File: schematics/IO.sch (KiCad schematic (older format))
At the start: 78 parts, among them J4 Outputs, J8 Power Pins, Q1 MMBT3906, U10 TL082, U11 6S21, U12 6S21, U13 TL082, U16 TL082, U6 DS1307Z+, U7 LM324, U8 TL082, U9 MCP4728, Y1 32.768 kHz

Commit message: fix: increased cutoff frequency
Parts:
- C23, C29: value 3p3 -> 0.5p
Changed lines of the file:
@@
 AR Path="/54260FB5/5441D502" Ref="C29"  Part="1"
 F 0 "C29" H 10075 2475 40  0000 L CNN
-F 1 "3p3" H 10081 2290 40  0000 L CNN
+F 1 "0.5p" H 10081 2290 40  0000 L CNN
 F 2 "Capacitors_SMD:C_0603" H 10113 2225 30  0001 C CNN
 F 3 "" H 10075 2375 60  0000 C CNN
@@
 AR Path="/54260FB5/55B7C49A" Ref="C23"  Part="1"
 F 0 "C23" H 10150 1175 40  0000 L CNN
-F 1 "3p3" H 10156 990 40  0000 L CNN
+F 1 "0.5p" H 10156 990 40  0000 L CNN
 F 2 "Capacitors_SMD:C_0603" H 10188 925 30  0001 C CNN
 F 3 "" H 10150 1075 60  0000 C CNN

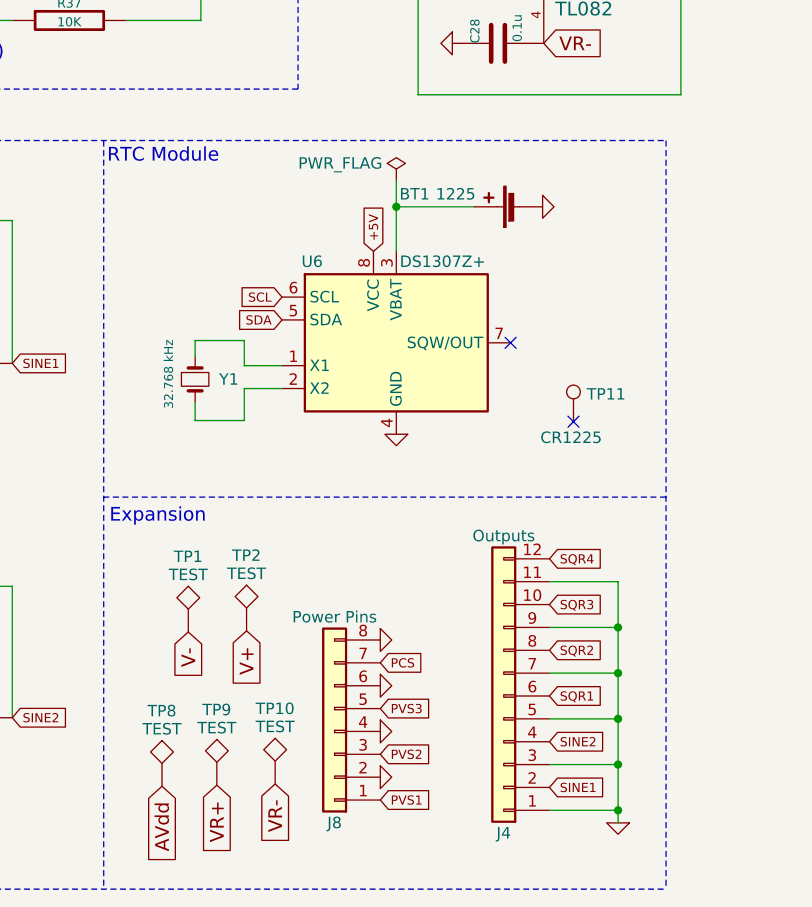
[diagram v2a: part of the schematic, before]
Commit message: feat: external power circuit schematics
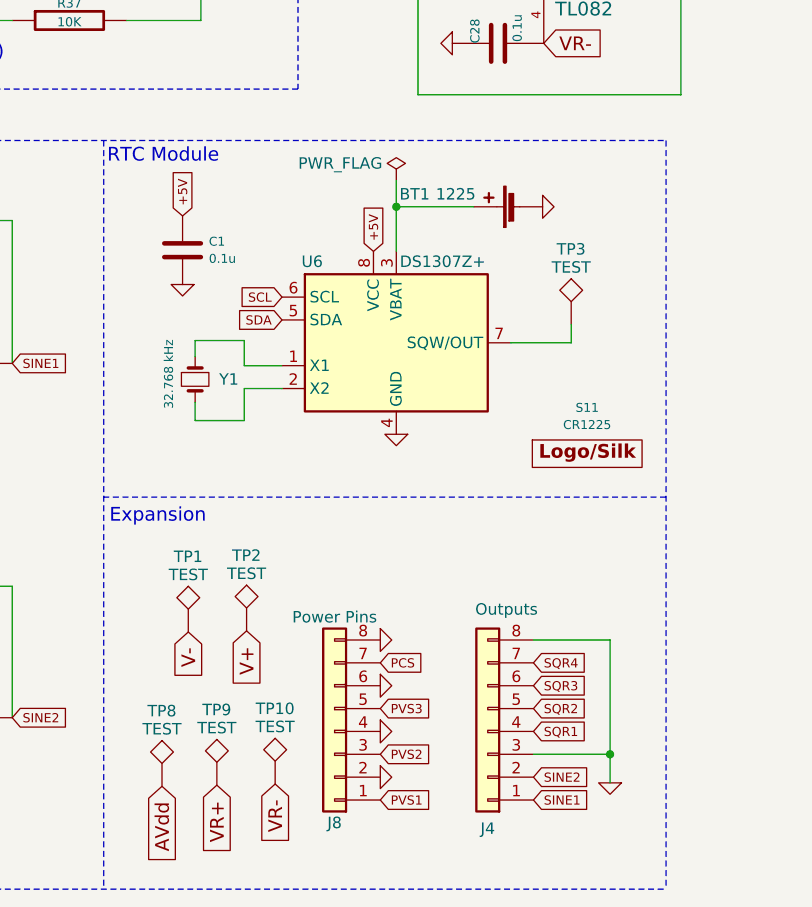
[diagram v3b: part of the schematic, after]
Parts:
- removed J4: Outputs, Pin_Headers:Pin_Header_Straight_1x12_Pitch2.54mm, symbol PSLab-rescue:Conn_01x12
- removed TP11: CR1225, Battery:Battery_CR1225, symbol Connector:TestPoint
- added C1: 0.1u, Capacitor_SMD:C_0603_1608Metric, symbol Device:C
- added J4: Outputs, Connector_PinSocket_2.54mm:PinSocket_1x08_P2.54mm_Vertical, symbol Connector_Generic:Conn_01x08
- added S11: CR1225, Battery:Battery_CR1225, symbol PSLab:Logos
- added TP3: TEST, TestPoint:TestPoint_Pad_1.0x1.0mm, symbol PSLab-rescue:TEST
- C22, C23, C24, C25, C26, C27, C28, C29, C30, C31, C32, C33, C34, C35, C36, C37, C38, C39, C40, C41, C43, C6, C7: footprint Capacitors_SMD:C_0603 -> Capacitor_SMD:C_0603_1608Metric
- R14, R15, R16, R17, R18, R19, R20, R21, R22, R23, R24, R25, R26, R27, R28, R29, R30, R31, R32, R33, R34, R35, R36, R37, R38, R39, R40, R41, R42, R43, R44, R45, R46, R47, R50: footprint Resistors_SMD:R_0603 -> Resistor_SMD:R_0603_1608Metric
- TP1, TP10, TP2, TP8, TP9: footprint Measurement_Points:Measurement_Point_Round-SMD-Pad_Small -> TestPoint:TestPoint_Pad_1.0x1.0mm
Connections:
- net +5V: now also C1.1
- net GND: now also C1.2, J4.3 (Pin_3), J4.8 (Pin_8)
- net SINE1: now also J4.1 (Pin_1)
- net SINE2: now also J4.2 (Pin_2)
- net SQR1: now also J4.4 (Pin_4)
- net SQR2: now also J4.5 (Pin_5)
- net SQR3: now also J4.6 (Pin_6)
- net SQR4: now also J4.7 (Pin_7)
- net at U6.7 (SQW/OUT): now also TP3.1
- no-connect marks 3 -> 1

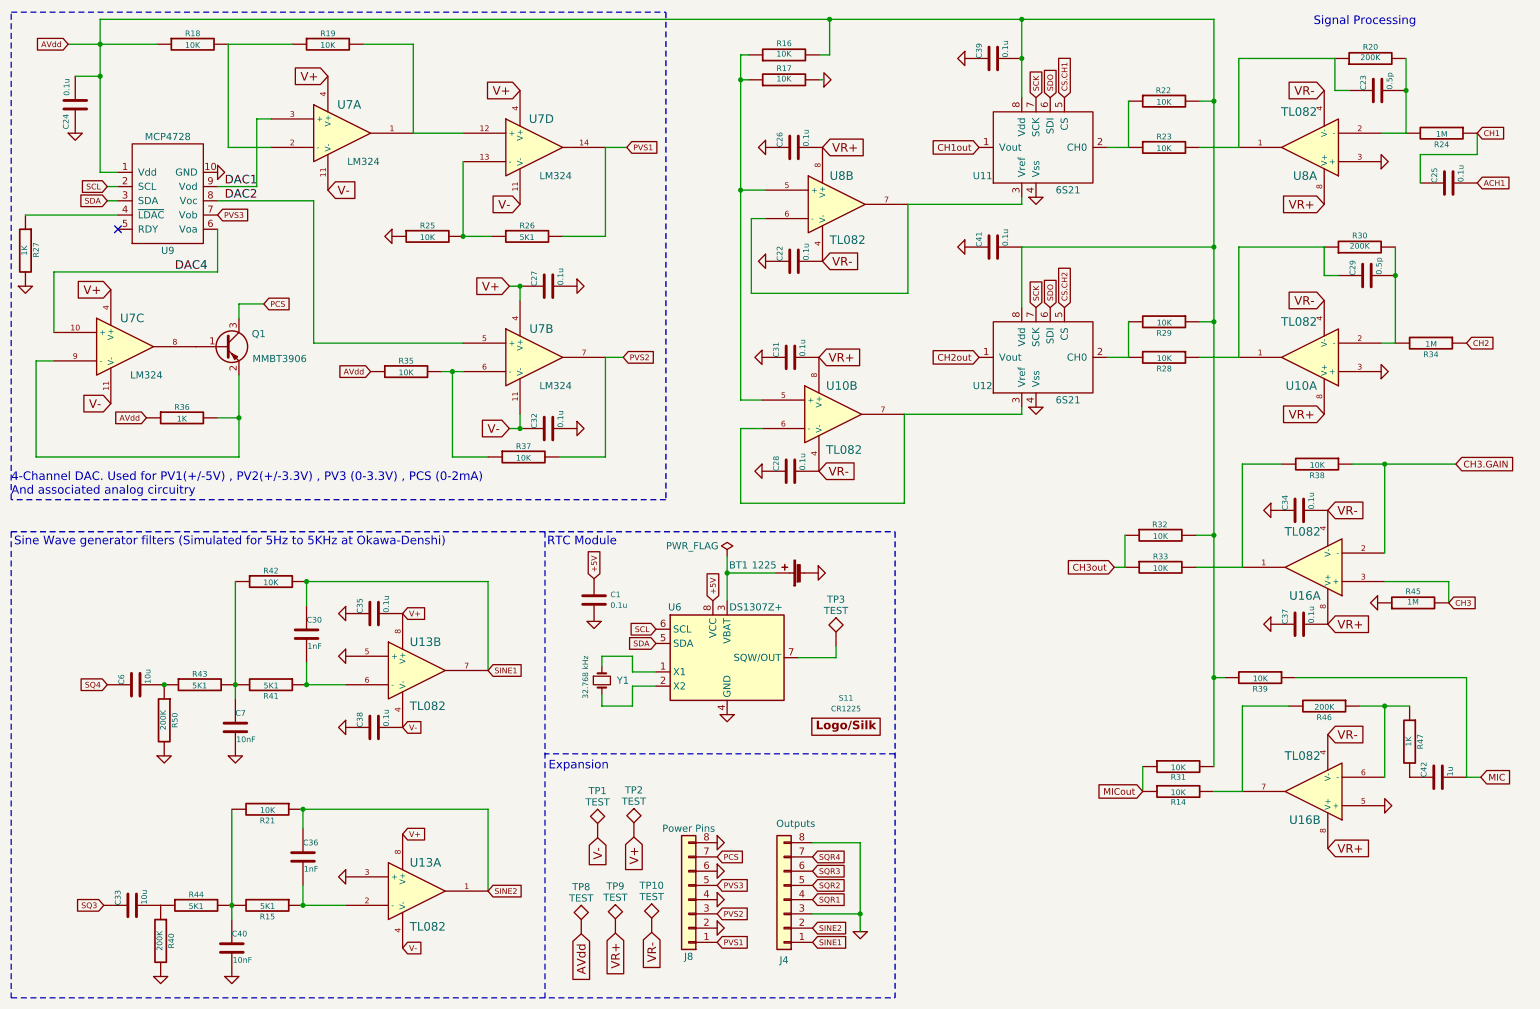
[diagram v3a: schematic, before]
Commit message: refactor: fixed rotation in resistors
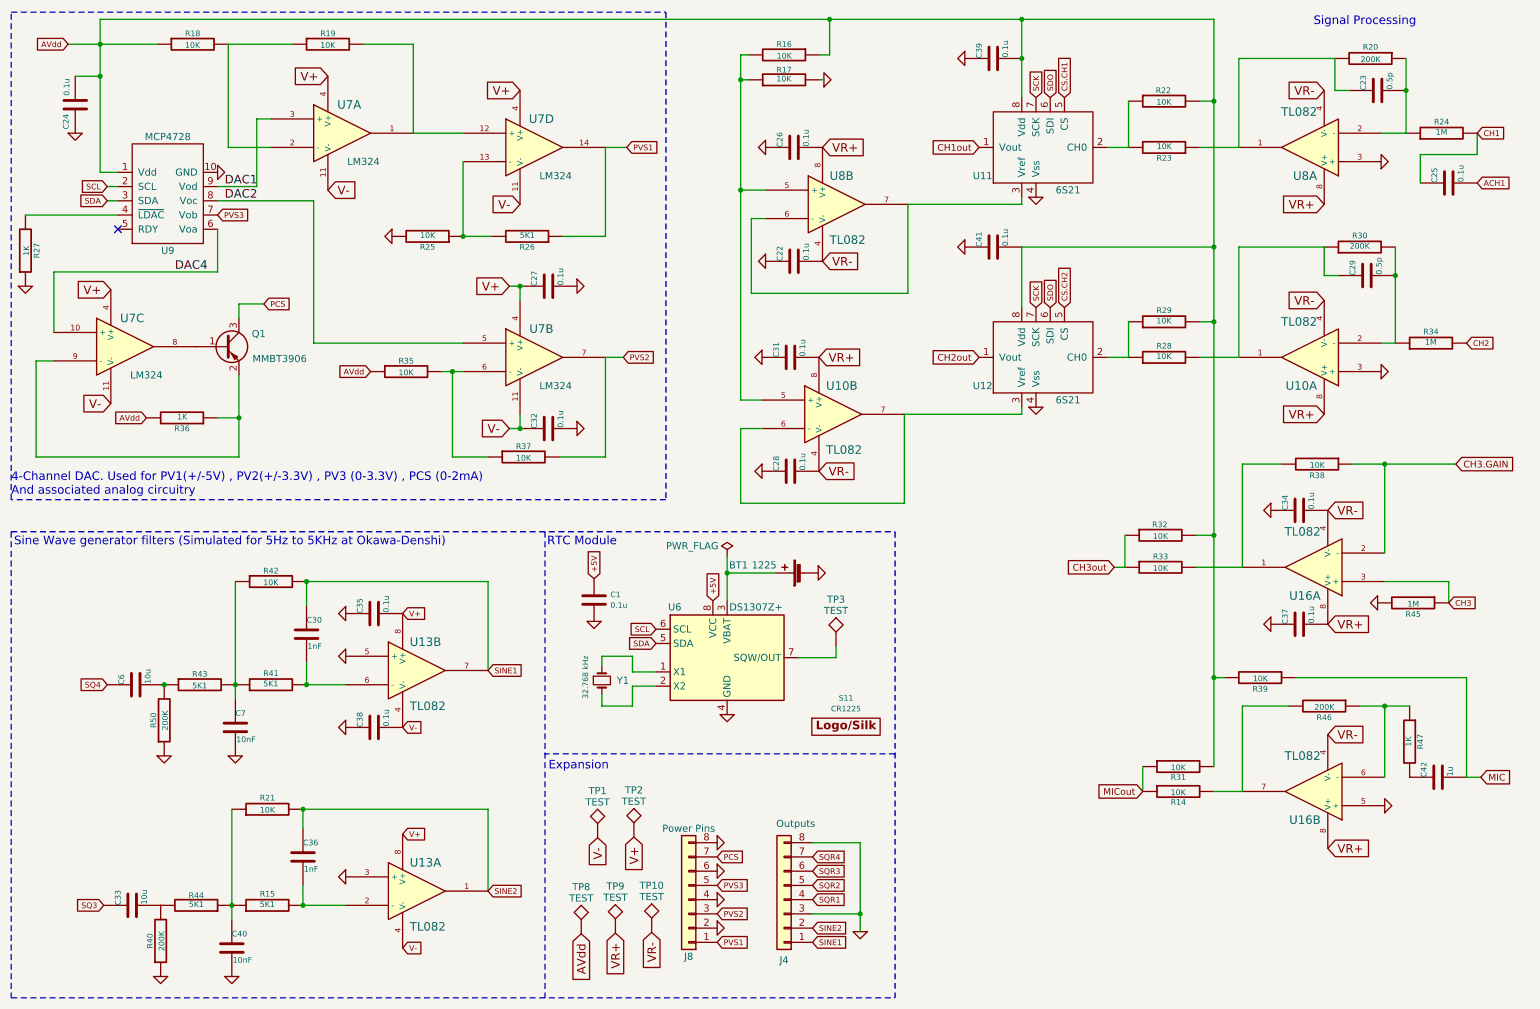
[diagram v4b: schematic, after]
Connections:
- net AVdd: now also R16.1, R29.2, R36.2; no longer R16.2, R29.1, R36.1
- net CH1: now also R24.2; no longer R24.1
- net CH2: now also R34.2; no longer R34.1
- net CH3: now also R45.1; no longer R45.2
- net GND: now also R25.2, R27.1, R40.1, R45.2, R50.1; no longer R25.1, R27.2, R40.2, R45.1, R50.2
- net PVS1: now also R26.1; no longer R26.2
- net SINE2: now also R21.2; no longer R21.1
- net at C29.1, R30.1, U10.1: now also R28.2; no longer R28.1
- net at C29.2, R30.2, U10.2 (-): now also R34.1; no longer R34.2
- net at R17.1, U10.5 (+), U8.5 (+): now also R16.2; no longer R16.1
- net at Q1.2 (E), U7.9 (-): now also R36.1; no longer R36.2
- net at U9.4 (~LDAC): now also R27.2; no longer R27.1
- net at C7.1, R42.1, R43.2: now also R41.1; no longer R41.2
- net at C6.2, R43.1: now also R50.2; no longer R50.1
- net at C23.1, U8.1: now also R20.2, R23.1; no longer R20.1, R23.2
- net at C23.2, U8.2 (-): now also R20.1, R24.1; no longer R20.2, R24.2
- net at R22.1, U11.2 (CH0): now also R23.2; no longer R23.1
- net at C30.2, U13.6 (-): now also R41.2; no longer R41.1
- net at C36.2, U13.2 (-): now also R15.2; no longer R15.1
- new net: R25.1, R26.2, U7.13 (-)
- new net: C33.2, R40.2, R44.2
- new net: C40.1, R15.1, R21.1, R44.1
- new net: R28.1, R29.1, U12.2 (CH0)
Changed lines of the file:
@@
 F 3 "" H 10525 2850 30  0000 C CNN
 	1    10525 2850
-	0    1    1    0
+	0    -1   -1   0
 $EndComp
 $Comp
@@
 AR Path="/555FFE64" Ref="R27"  Part="1"
 AR Path="/54260FB5/555FFE64" Ref="R27"  Part="1"
-F 0 "R27" V 575 2205 40  0000 C CNN
+F 0 "R27" V 730 2200 40  0000 C CNN
 F 1 "1K" V 657 2201 40  0000 C CNN
 F 2 "Resistor_SMD:R_0603_1608Metric" V 580 2200 30  0001 C CNN
 F 3 "" H 650 2200 30  0000 C CNN
 	1    650  2200
-	-1   0    0    -1
+	1    0    0    1
 $EndComp
 Text GLabel 950  750  0    40   Input ~ 0
@@
 F 3 "" H 4175 2100 30  0000 C CNN
 	1    4175 2100
-	0    -1   1    0
+	0    1    -1   0
 $EndComp
 $Comp
@@
 F 3 "" H 3475 2100 30  0000 C CNN
 	1    3475 2100
-	0    -1   1    0
+	0    1    -1   0
 $EndComp
 $Comp
@@
 F 3 "" H 1750 3375 30  0000 C CNN
 	1    1750 3375
-	0    -1   1    0
+	0    1    -1   0
 $EndComp
 Text GLabel 1500 3375 0    40   Input ~ 0
@@
 F 3 "" H 1600 7050 30  0000 C CNN
 	1    1600 7050
-	-1   0    0    -1
+	1    0    0    1
 $EndComp
 $Comp
@@
 AR Path="/556399B0" Ref="R44"  Part="1"
 AR Path="/54260FB5/556399B0" Ref="R44"  Part="1"
-F 0 "R44" V 1775 6800 40  0000 C CNN
+F 0 "R44" V 1920 6800 40  0000 C CNN
 F 1 "5K1" V 1857 6801 40  0000 C CNN
 F 2 "Resistor_SMD:R_0603_1608Metric" V 1780 6800 30  0001 C CNN
 F 3 "" H 1850 6800 30  0000 C CNN
 	1    1850 6800
-	0    -1   1    0
+	0    1    -1   0
 $EndComp
 $Comp
@@
 F 3 "" H 8650 2950 30  0000 C CNN
 	1    8650 2950
-	0    1    1    0
+	0    -1   -1   0
 $EndComp
 $Comp
@@
 F 3 "" H 8650 2700 30  0000 C CNN
 	1    8650 2700
-	0    1    1    0
+	0    -1   -1   0
 $EndComp
 $Comp
@@
 AR Path="/55B7C46A" Ref="R20"  Part="1"
 AR Path="/54260FB5/55B7C46A" Ref="R20"  Part="1"
-F 0 "R20" V 10180 850 40  0000 C CNN
+F 0 "R20" V 10020 850 40  0000 C CNN
 F 1 "200K" V 10107 851 40  0000 C CNN
 F 2 "Resistor_SMD:R_0603_1608Metric" V 10030 850 30  0001 C CNN
 F 3 "" H 10100 850 30  0000 C CNN
 	1    10100 850
-	0    -1   -1   0
+	0    1    1    0
 $EndComp
 $Comp
@@
 F 3 "" H 10600 1375 30  0000 C CNN
 	1    10600 1375
-	0    1    1    0
+	0    -1   -1   0
 $EndComp
 $Comp
@@
 F 3 "" H 8650 1475 30  0000 C CNN
 	1    8650 1475
-	0    -1   1    0
+	0    1    -1   0
 $EndComp
 $Comp
@@
 AR Path="/55B7C4D5" Ref="R16"  Part="1"
 AR Path="/54260FB5/55B7C4D5" Ref="R16"  Part="1"
-F 0 "R16" V 6060 825 40  0000 C CNN
+F 0 "R16" V 5905 825 40  0000 C CNN
 F 1 "10K" V 5987 826 40  0000 C CNN
 F 2 "Resistor_SMD:R_0603_1608Metric" V 5910 825 30  0001 C CNN
 F 3 "" H 5980 825 30  0000 C CNN
 	1    5980 825
-	0    -1   -1   0
+	0    1    1    0
 $EndComp
 $Comp
@@
 AR Path="/55B7C4E5" Ref="R17"  Part="1"
 AR Path="/54260FB5/55B7C4E5" Ref="R17"  Part="1"
-F 0 "R17" V 6060 1000 40  0000 C CNN
+F 0 "R17" V 6050 1000 40  0000 C CNN
 F 1 "10K" V 5987 1001 40  0000 C CNN
 F 2 "Resistor_SMD:R_0603_1608Metric" V 5910 1000 30  0001 C CNN
@@
 AR Path="/54260FB5/55B7C4EE" Ref="R21"  Part="1"
 F 0 "R21" V 2430 6125 40  0000 C CNN
-F 1 "10K" V 2357 6126 40  0000 C CNN
+F 1 "10K" V 2345 6125 40  0000 C CNN
 F 2 "Resistor_SMD:R_0603_1608Metric" V 2280 6125 30  0001 C CNN
 F 3 "" H 2350 6125 30  0000 C CNN
 	1    2350 6125
-	0    1    1    0
+	0    -1   -1   0
 $EndComp
 $Comp
@@
 F 3 "" H 2375 5250 30  0000 C CNN
 	1    2375 5250
-	0    1    1    0
+	0    -1   -1   0
 $EndComp
 Text GLabel 10700 3700 2    47   Input ~ 0
@@
 F 3 "" H 10400 4675 30  0000 C CNN
 	1    10400 4675
-	0    -1   -1   0
+	0    1    1    0
 $EndComp
 $Comp
@@
 F 3 "" H 2350 6800 30  0000 C CNN
 	1    2350 6800
-	0    1    1    0
+	0    -1   -1   0
 $EndComp
 Text Label 2050 1750 0    60   ~ 0
@@
 F 3 "" H 1625 5500 30  0000 C CNN
 	1    1625 5500
-	-1   0    0    -1
-$EndComp
-$Comp
+	1    0    0    1
+$EndComp
+$Comp

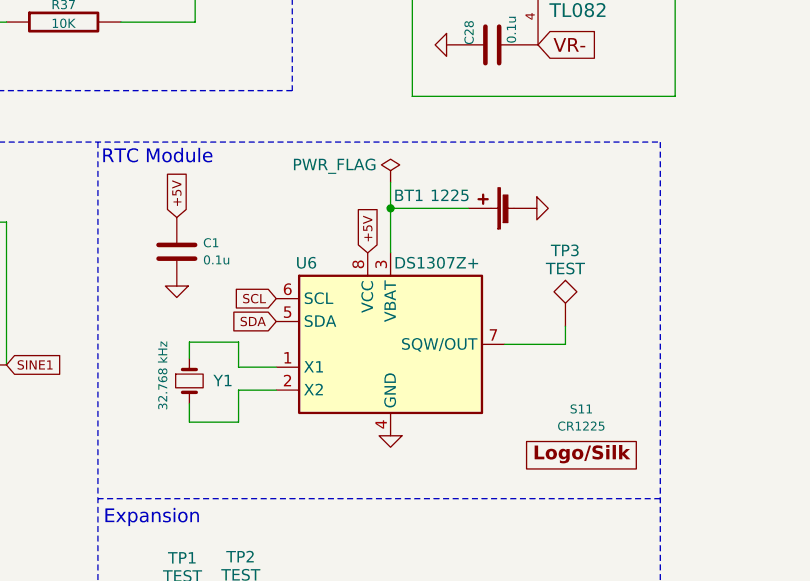
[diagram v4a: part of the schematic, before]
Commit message: feat: bom generator and updated project to support bom generator
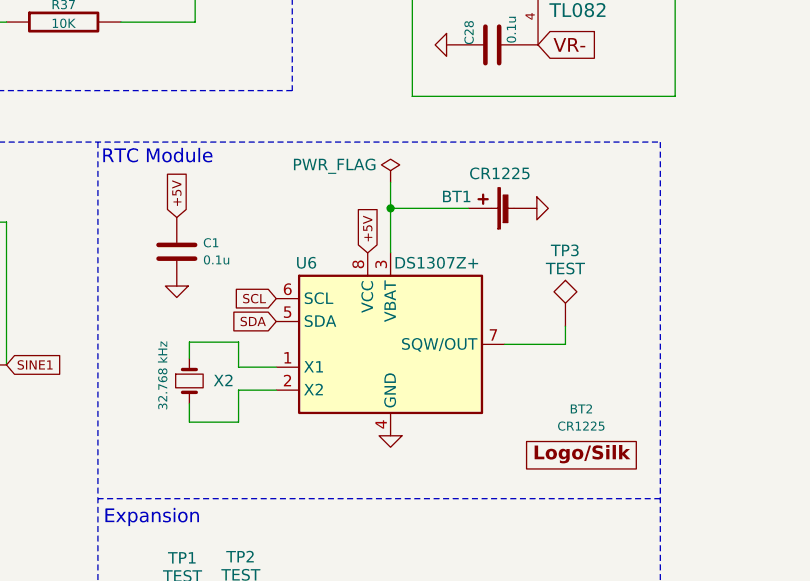
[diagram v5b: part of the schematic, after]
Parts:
- BT1: value 1225 -> CR1225; Description (none) -> Coin cell battery holder (CR1225/1216); Mfr No. (none) -> BAT-HLD-012-SMT; PartNumber (none) -> BAT-HLD-012-SMT; Price (none) -> 0.29
- BT2: renamed from S11; Description (none) -> 3V 12.5mm x 2.5 mm 48 mAh; PartNumber (none) -> CR1225; Price (none) -> 1
- C1, C22, C24, C25, C26, C27, C28, C31, C32, C34, C35, C37, C38, C39, C41: Description (none) -> 16V 10%; Mfr No. (none) -> C0603C104J4RACTU; PartNumber (none) -> C0603C104J4RACTU; Price (none) -> 0.15
- C23, C29: Description (none) -> 16V 20%; Mfr No. (none) -> VJ0603A0R5BXJCW1BC; PartNumber (none) -> VJ0603A0R5BXJCW1BC; Price (none) -> 0.45
- C30, C36: Description (none) -> 16V 5%; Mfr No. (none) -> C0603C102J5RACAUTO; PartNumber (none) -> C0603C102J5RACAUTO; Price (none) -> 0.12
- C33, C6: Description (none) -> 16V 20%; Mfr No. (none) -> EMK107BC6106MA-T; PartNumber (none) -> EMK107BC6106MA-T; Price (none) -> 0.46
- C40, C7: Description (none) -> 16V 5%; Mfr No. (none) -> VJ0603Y103JXJPW1BC; PartNumber (none) -> VJ0603Y103JXJPW1BC; Price (none) -> 0.37
- C43: Description (none) -> 16V 20%; Mfr No. (none) -> 0603YD105KAT2A; PartNumber (none) -> 0603YD105KAT2A; Price (none) -> 0.18
- J4, J8: Description (none) -> Straight female 2.54 mm 1row; Mfr No. (none) -> SSW-108-01-T-S; PartNumber (none) -> SSW-108-01-T-S; Price (none) -> 0.82
- Q1: Description (none) -> 45V Vce, 0.8A Ic, PNP, SOT-23; Mfr No. (none) -> MMBT3906-7-F; PartNumber (none) -> MMBT3906-7-F; Price (none) -> 0.11
- R14, R16, R17, R18, R19, R21, R22, R23, R25, R28, R29, R31, R32, R33, R35, R37, R38, R39, R42: Description (none) -> 1/16W 5%; Mfr No. (none) -> RR0816P-103-D; PartNumber (none) -> RR0816P-103-D; Price (none) -> 0.12
- R15, R26, R41, R43, R44: Description (none) -> 1/16W 5%; Mfr No. (none) -> RR0816P-512-D; PartNumber (none) -> RR0816P-512-D; Price (none) -> 0.1
- R20, R30, R40, R46, R50: Description (none) -> 1/16W 5%; Mfr No. (none) -> RR0816P-204-D; PartNumber (none) -> RR0816P-204-D; Price (none) -> 0.1
- R24, R34, R45: Description (none) -> 1/16W 5%; Mfr No. (none) -> RT0603FRE071ML; PartNumber (none) -> RT0603FRE071ML; Price (none) -> 0.1
- R27, R36, R47: Description (none) -> 1/16W 5%; Mfr No. (none) -> RR0816P-102-D; PartNumber (none) -> RR0816P-102-D; Price (none) -> 0.12
- U10, U13, U16, U8: Description (none) -> SOIC 8; Mfr No. (none) -> TL082CDR; PartNumber (none) -> TL082CDR; Price (none) -> 0.41
- U11, U12: Description (none) -> SOIC 8; Mfr No. (none) -> MCP6S21-I/SN; PartNumber (none) -> MCP6S21-I/SN; Price (none) -> 1.1
- U6: Description (none) -> Real Time Clock IC; Mfr No. (none) -> DS1307Z+; PartNumber (none) -> DS1307Z+; Price (none) -> 3.69
- U7: Description (none) -> SOIC 14; Mfr No. (none) -> LM324D; PartNumber (none) -> LM324D; Price (none) -> 0.42
- U9: Description (none) -> MSOP 10; Mfr No. (none) -> MCP4728-E/UN; PartNumber (none) -> MCP4728-E/UN; Price (none) -> 1.89
- X2: renamed from Y1; Description (none) -> RTC Crystal 32.768 kHz; Mfr No. (none) -> ABS07-166-32.768KHZ-T; PartNumber (none) -> ABS07-166-32.768KHZ-T; Price (none) -> 0.66
